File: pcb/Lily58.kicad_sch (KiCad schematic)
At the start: 111 parts, among them P4 OLED, SW1 SW_PUSH, SW10 SW_PUSH, SW11 SW_PUSH, SW12 SW_PUSH, SW13 SW_PUSH, SW14 SW_PUSH, SW15 SW_PUSH, SW16 SW_PUSH, SW17 SW_PUSH, SW18 SW_PUSH, SW19 SW_PUSH, SW2 SW_PUSH, SW20 SW_PUSH, SW21 SW_PUSH, SW22 SW_PUSH, SW23 SW_PUSH, SW24 SW_PUSH, SW25 Rotary_Encoder_Switch, SW25b1 SW_PUSH, SW26 SW_PUSH, SW27 SW_PUSH, SW28 SW_PUSH, SW29 SW_PUSH, SW3 SW_PUSH, SW4 SW_PUSH, SW5 SW_PUSH, SW6 SW_PUSH, SW7 SW_PUSH, SW8 SW_PUSH, SW9 SW_PUSH, U1 NiceNano

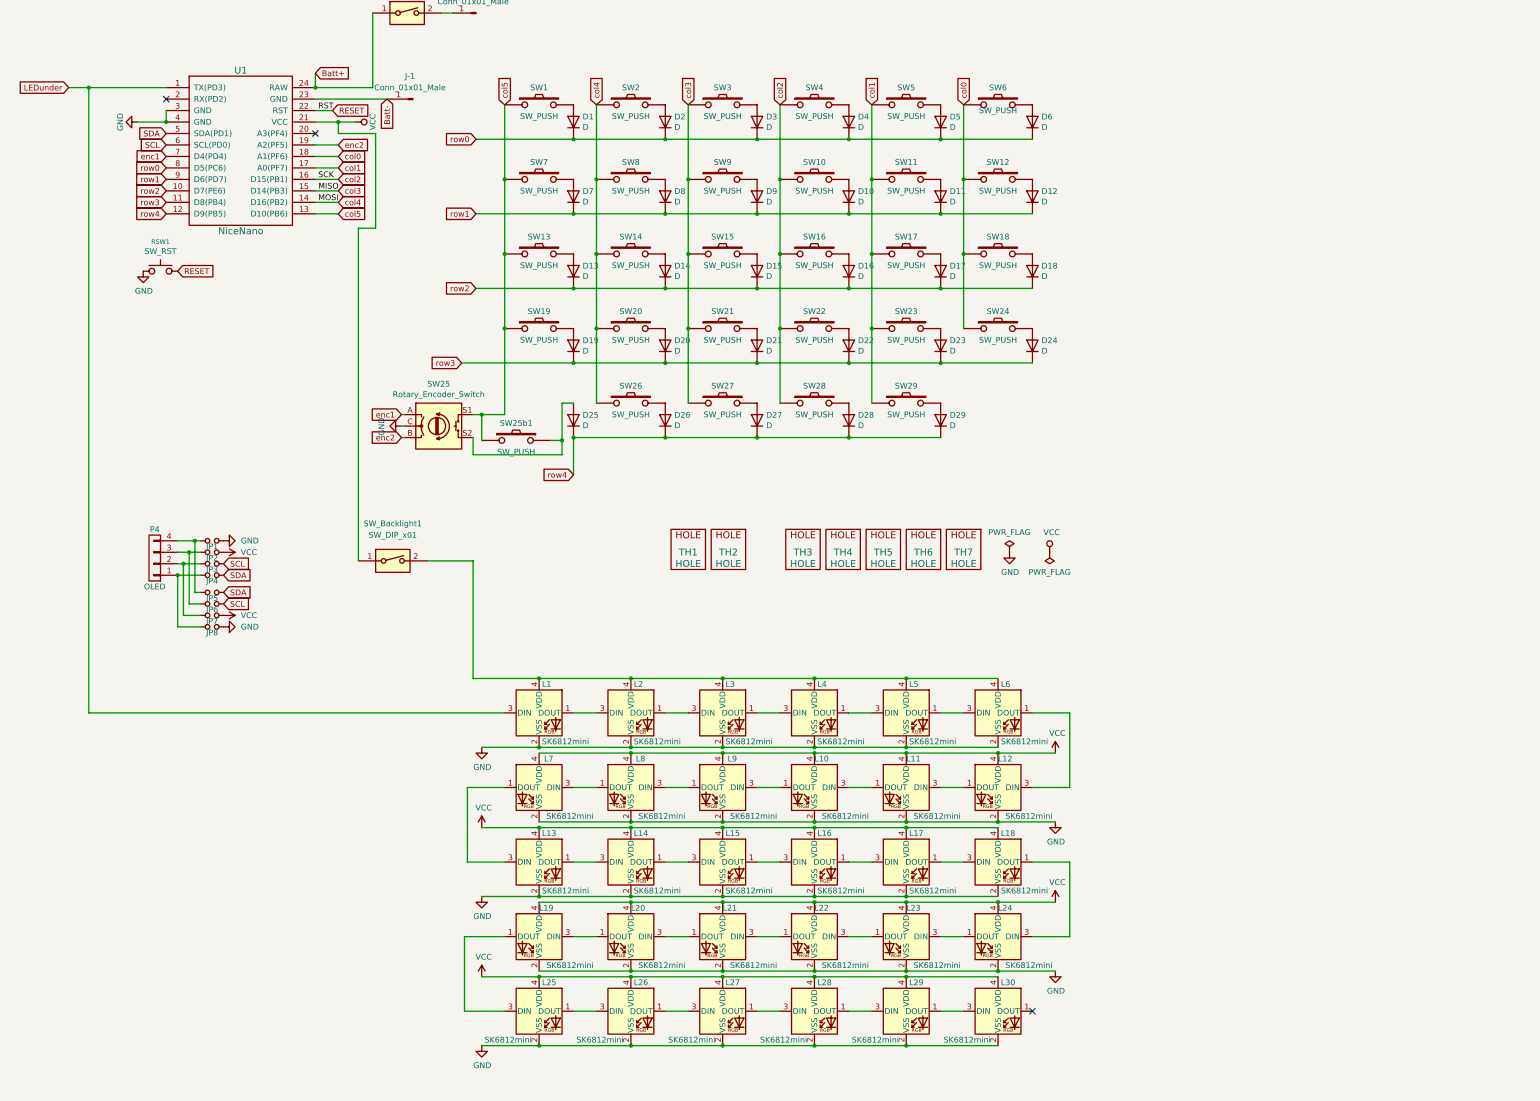
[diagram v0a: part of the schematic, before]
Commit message: Some edits
Added in underglow LEDs to the schematics, started moving around the PCB items.
Deciding between TH and SMD diodes (or both)
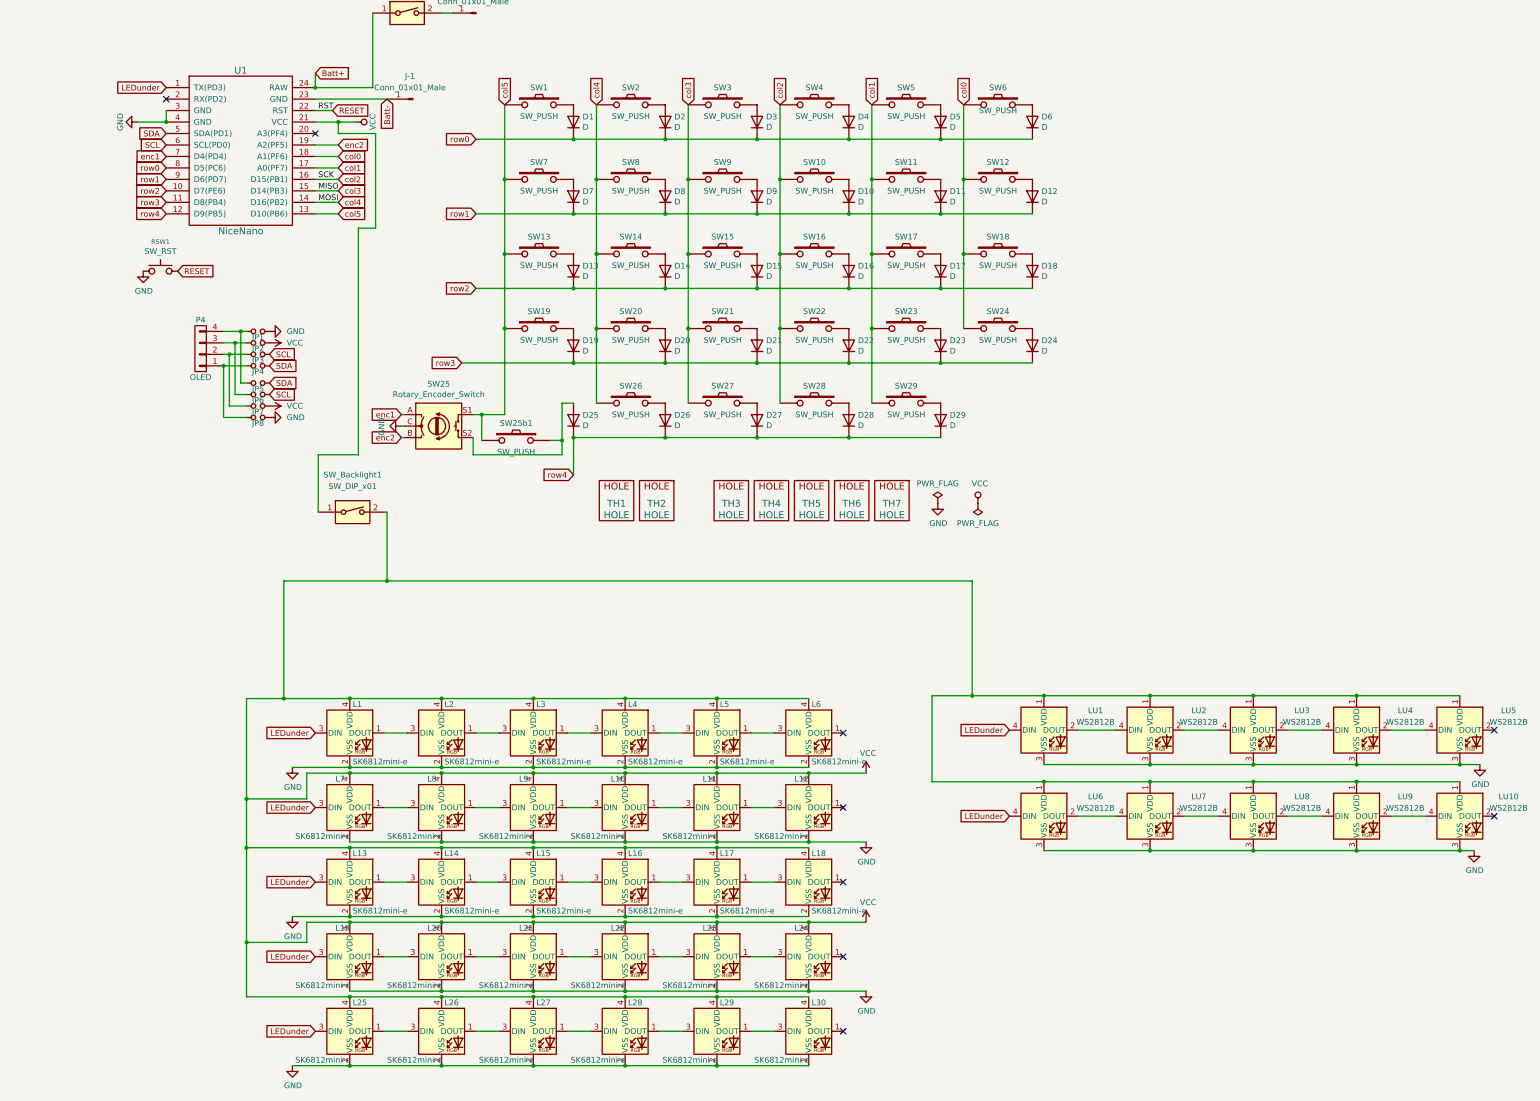
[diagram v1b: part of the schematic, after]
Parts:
- added LU1, LU10, LU2, LU3, LU4, LU5, LU6, LU7, LU8, LU9: WS2812B, LED_SMD:LED_WS2812B_PLCC4_5.0x5.0mm_P3.2mm, symbol LED:WS2812B
- L1, L10, L11, L12, L13, L14, L15, L16, L17, L18, L19, L2, L20, L21, L22, L23, L24, L25, L26, L27, L28, L29, L3, L30, L4, L5, L6, L7, L8, L9: value SK6812mini -> SK6812mini-e
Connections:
- net GND: now also LU1.3 (VSS), LU10.3 (VSS), LU2.3 (VSS), LU3.3 (VSS), LU4.3 (VSS), LU5.3 (VSS), LU6.3 (VSS), LU7.3 (VSS), LU8.3 (VSS), LU9.3 (VSS)
- net LEDunder: now also L13.3 (DIN), L19.3 (DIN), L25.3 (DIN), L7.3 (DIN), LU1.4 (DIN), LU6.4 (DIN)
- net VCC: now also L1.4 (VDD), L2.4 (VDD), L3.4 (VDD), L4.4 (VDD), L5.4 (VDD), L6.4 (VDD), SW_Backlight1.2, LU1.1 (VDD), LU10.1 (VDD), LU2.1 (VDD), LU3.1 (VDD), LU4.1 (VDD), LU5.1 (VDD), LU6.1 (VDD), LU7.1 (VDD), LU8.1 (VDD), LU9.1 (VDD)
- net at L6.1 (DOUT): no longer L12.3 (DIN)
- net at L7.1 (DOUT): now also L8.3 (DIN); no longer L13.3 (DIN)
- net at L8.1 (DOUT): now also L9.3 (DIN); no longer L7.3 (DIN)
- net at L9.1 (DOUT): now also L10.3 (DIN); no longer L8.3 (DIN)
- net at L10.1 (DOUT): now also L11.3 (DIN); no longer L9.3 (DIN)
- net at L11.1 (DOUT): now also L12.3 (DIN); no longer L10.3 (DIN)
- net at L12.1 (DOUT): no longer L11.3 (DIN)
- net at L18.1 (DOUT): no longer L24.3 (DIN)
- net at L19.1 (DOUT): now also L20.3 (DIN); no longer L25.3 (DIN)
- net at L20.1 (DOUT): now also L21.3 (DIN); no longer L19.3 (DIN)
- net at L21.1 (DOUT): now also L22.3 (DIN); no longer L20.3 (DIN)
- net at L22.1 (DOUT): now also L23.3 (DIN); no longer L21.3 (DIN)
- net at L23.1 (DOUT): now also L24.3 (DIN); no longer L22.3 (DIN)
- net at L24.1 (DOUT): no longer L23.3 (DIN)
- new net: LU8.2 (DOUT), LU9.4 (DIN)
- new net: LU7.2 (DOUT), LU8.4 (DIN)
- new net: LU4.2 (DOUT), LU5.4 (DIN)
- new net: LU3.2 (DOUT), LU4.4 (DIN)
- new net: LU1.2 (DOUT), LU2.4 (DIN)
- new net: LU2.2 (DOUT), LU3.4 (DIN)
- new net: LU10.4 (DIN), LU9.2 (DOUT)
- new net: LU6.2 (DOUT), LU7.4 (DIN)
- no-connect marks 3 -> 9
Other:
- moved on the sheet: JP1, JP2, JP3, JP4, JP5, JP6, JP7, JP8, L1, L10, L11, L12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

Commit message: More PCB edits
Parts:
- D1, D10, D11, D12, D13, D14, D15, D16, D17, D18, D19, D2, D20, D21, D22, D23, D24, D25, D26, D27, D28, D29, D3, D4, D5, D6, D7, D8, D9: footprint Lily58-footprint:Diode_TH_SOD123 -> Lily58-footprint:D_SOD-123-Pretty

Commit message: Split keyboard PCB, remove LEDs
Split the keyboard PCBs so it is no longer double sided, removed per-key lighting for this iteration due to ZMK support. Thinking about RP2040+wireless for a future iteration to add per-key lighting back in
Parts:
- removed JP5, JP6, JP7, JP8: Jumper_NO_Small, Lily58-footprint:Jumper, symbol Device:Jumper_NO_Small
- removed L1, L10, L11, L12, L13, L14, L15, L16, L17, L18, L19, L2, L20, L21, L22, L23, L24, L25, L26, L27, L28, L29, L3, L30, L4, L5, L6, L7, L8, L9: SK6812mini-e, LED_SMD:SK6812-MINI-E, symbol LED:SK6812MINI
- removed SW_Backlight1: SW_DIP_x01, Button_Switch_THT:SW_CuK_OS102011MA1QN1_SPDT_Angled, symbol Switch:SW_DIP_x01
- added D31, D32, D33, D34, D35, D36, D37, D38, D39, D40, D41, D42, D43, D44, D45, D46, D47, D48, D49, D50, D51, D52, D53, D54, D55, D56, D57, D58, D59: D, Lily58-footprint:D_SOD-123-Pretty, symbol Lily58-rescue:D-Lily58-cache
- added J+2: Conn_01x01_Malel1, TestPoint:TestPoint_Pad_2.0x2.0mm, symbol Connector:Conn_01x01_Male
- added J-2: Conn_01x01_Malel2, TestPoint:TestPoint_Pad_2.0x2.0mm, symbol Connector:Conn_01x01_Male
- added JP14, JP15, JP16, JP17, JP18, JP9: Jumper_NO_Small, Lily58-footprint:Jumper, symbol Device:Jumper_NO_Small
- added LU11, LU12, LU13, LU14, LU15, LU16, LU17, LU18, LU19, LU20: WS2812B, LED_SMD:LED_WS2812B_PLCC4_5.0x5.0mm_P3.2mm, symbol LED:WS2812B
- added P2: OLED, Lily58-footprint:MY_SIL-4, symbol Lily58-rescue:CONN_01X04-Lily58-cache
- added RSW2: SW_RST, Lily58-footprint:TACT_SWITCH_TVBP06, symbol Lily58-rescue:SW_RST-Lily58-cache
- added SW31, SW32, SW33, SW34, SW35, SW36, SW37, SW38, SW39, SW40, SW41, SW42, SW43, SW44, SW45, SW46, SW47, SW48, SW49, SW50, SW51, SW52, SW53, SW54, SW56, SW57, SW58, SW59: SW_PUSH, Lily58-footprint:MX_Socket_18mm, symbol Lily58-rescue:SW_PUSH-Lily58-cache
- added SW55: Rotary_Encoder_Switch, Lily58-footprint:RotaryEncoder_Alps_EC11E-Switch_Vertical_H20mm, symbol Device:Rotary_Encoder_Switch
- added SW_BatteryL1: SW_DIP_x01, Button_Switch_THT:SW_CuK_OS102011MA1QN1_SPDT_Angled, symbol Switch:SW_DIP_x01
- added TH10, TH11, TH12, TH13, TH14: HOLE, Lily58-footprint:HOLE_M2_TH, symbol Lily58-rescue:HOLE-Lily58-cache
- added TH8, TH9: HOLE, Lily58-footprint:HOLE_M2, symbol Lily58-rescue:HOLE-Lily58-cache
- added U2: NiceNano, nice-nano-kicad:nice_nano, symbol Lily58-rescue:ProMicro_2-Lily58-cache
- J+1: value Conn_01x01_Male -> Conn_01x01_Maler1
- J-1: value Conn_01x01_Male -> Conn_01x01_Maler2
- renumbered P4 to P1, SW_Battery1 to SW_BatteryR1
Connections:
- net GND: now also JP17.2, LU11.3 (VSS), LU12.3 (VSS), LU13.3 (VSS), LU14.3 (VSS), LU15.3 (VSS), LU16.3 (VSS), LU17.3 (VSS), LU18.3 (VSS), LU19.3 (VSS), LU20.3 (VSS), RSW2.1, SW55.C, U2.3 (GND), U2.4 (GND)
- net VCC: now also JP16.2, JP18.2, JP9.2, U2.21 (VCC); no longer LU1.1 (VDD), LU10.1 (VDD), LU2.1 (VDD), LU3.1 (VDD), LU4.1 (VDD), LU5.1 (VDD), LU6.1 (VDD), LU7.1 (VDD), LU8.1 (VDD), LU9.1 (VDD)
- net at LU5.2 (DOUT): now also LU6.4 (DIN)
- net Batt+ renamed Batt+r
- net Batt- renamed Batt-r
- net LEDunder renamed LEDunderR
- net LEDunderR: no longer LU6.4 (DIN)
- net RESET renamed RESETR
- net SCL renamed SCLr
- net SDA renamed SDAr
- net col2 renamed col12
- net col12: now also SW34.1, SW40.1, SW46.1, SW52.1, SW58.1, U2.16 (D15(PB1))
- net col3 renamed col13
- net col13: now also SW33.1, SW39.1, SW45.1, SW51.1, SW57.1, U2.15 (D14(PB3))
- net col4 renamed col14
- net col14: now also SW32.1, SW38.1, SW44.1, SW50.1, SW56.1, U2.14 (D16(PB2))
- new net: D59.2 (A), SW59.2
- new net: D35.2 (A), SW35.2
- new net: D42.2 (A), SW42.2
- new net: JP9.1, LU1.1 (VDD), LU10.1 (VDD), LU2.1 (VDD), LU3.1 (VDD), LU4.1 (VDD), LU5.1 (VDD), LU6.1 (VDD), LU7.1 (VDD), LU8.1 (VDD), LU9.1 (VDD)
- new net: JP14.1, P2.4 (P4)
- new net: D37.2 (A), SW37.2
- new net: D54.2 (A), SW54.2
- new net: D58.2 (A), SW58.2
- new net: D50.2 (A), SW50.2
- new net: D39.2 (A), SW39.2
- new net: D38.2 (A), SW38.2
- new net: D52.2 (A), SW52.2
- new net: D40.2 (A), SW40.2
- new net: D55.2 (A), SW55.S2
- new net: JP18.1, LU11.1 (VDD), LU12.1 (VDD), LU13.1 (VDD), LU14.1 (VDD), LU15.1 (VDD), LU16.1 (VDD), LU17.1 (VDD), LU18.1 (VDD), LU19.1 (VDD), LU20.1 (VDD)
- new net: D53.2 (A), SW53.2
- new net: D41.2 (A), SW41.2
- new net: D44.2 (A), SW44.2
- new net: D56.2 (A), SW56.2
- new net: D33.2 (A), SW33.2
- new net: D47.2 (A), SW47.2
- new net: JP17.1, P2.1 (P1)
- new net: JP16.1, P2.2 (P2)
- new net: JP15.1, P2.3 (P3)
- new net: D46.2 (A), SW46.2
- new net: LU18.2 (DOUT), LU19.4 (DIN)
- new net: LU17.2 (DOUT), LU18.4 (DIN)
- new net: LU11.2 (DOUT), LU12.4 (DIN)
- new net: D36.2 (A), SW36.2
- new net: D43.2 (A), SW43.2
- new net: LU19.2 (DOUT), LU20.4 (DIN)
- new net: D49.2 (A), SW49.2
- new net: J+2.1 (Pin_1), SW_BatteryL1.2
- new net: D51.2 (A), SW51.2
- new net: LU12.2 (DOUT), LU13.4 (DIN)
- new net: LU16.2 (DOUT), LU17.4 (DIN)
- new net: LU15.2 (DOUT), LU16.4 (DIN)
- new net: LU14.2 (DOUT), LU15.4 (DIN)
- new net: D32.2 (A), SW32.2
- new net: D34.2 (A), SW34.2
- new net: D48.2 (A), SW48.2
- new net: D57.2 (A), SW57.2
- new net: D45.2 (A), SW45.2
- new net: LU13.2 (DOUT), LU14.4 (DIN)
- new net: D31.2 (A), SW31.2
- new net Batt+l: SW_BatteryL1.1, U2.24 (RAW)
- new net Batt-l: J-2.1 (Pin_1), U2.23 (GND)
- new net LEDunderL: LU11.4 (DIN), U2.1 (TX(PD3))
- new net RESETL: RSW2.2, U2.22 (RST)
- new net SCLl: JP15.2, U2.6 (SCL(PD0))
- new net SDAl: JP14.2, U2.5 (SDA(PD1))
- new net col10: SW36.1, SW42.1, SW48.1, SW54.1, U2.18 (A1(PF6))
- new net col11: SW35.1, SW41.1, SW47.1, SW53.1, SW59.1, U2.17 (A0(PF7))
- new net col15: SW31.1, SW37.1, SW43.1, SW49.1, SW55.S1, U2.13 (D10(PB6))
- new net enc3: SW55.A, U2.7 (D4(PD4))
- new net enc4: SW55.B, U2.19 (A2(PF5))
- new net row10: D31.1 (K), D32.1 (K), D33.1 (K), D34.1 (K), D35.1 (K), D36.1 (K), U2.8 (D5(PC6))
- new net row11: D37.1 (K), D38.1 (K), D39.1 (K), D40.1 (K), D41.1 (K), D42.1 (K), U2.9 (D6(PD7))
- new net row12: D43.1 (K), D44.1 (K), D45.1 (K), D46.1 (K), D47.1 (K), D48.1 (K), U2.10 (D7(PE6))
- new net row13: D49.1 (K), D50.1 (K), D51.1 (K), D52.1 (K), D53.1 (K), D54.1 (K), U2.11 (D8(PB4))
- new net row14: D55.1 (K), D56.1 (K), D57.1 (K), D58.1 (K), D59.1 (K), U2.12 (D9(PB5))
- no-connect marks 9 -> 6
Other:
- moved on the sheet: LU1, LU10, LU2, LU3, LU4, LU5, LU6, LU7, LU8, LU9
